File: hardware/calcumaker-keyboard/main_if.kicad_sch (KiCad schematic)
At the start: 2 parts, among them J1 TO MCU (stack), J3 TO MCU (FFC)

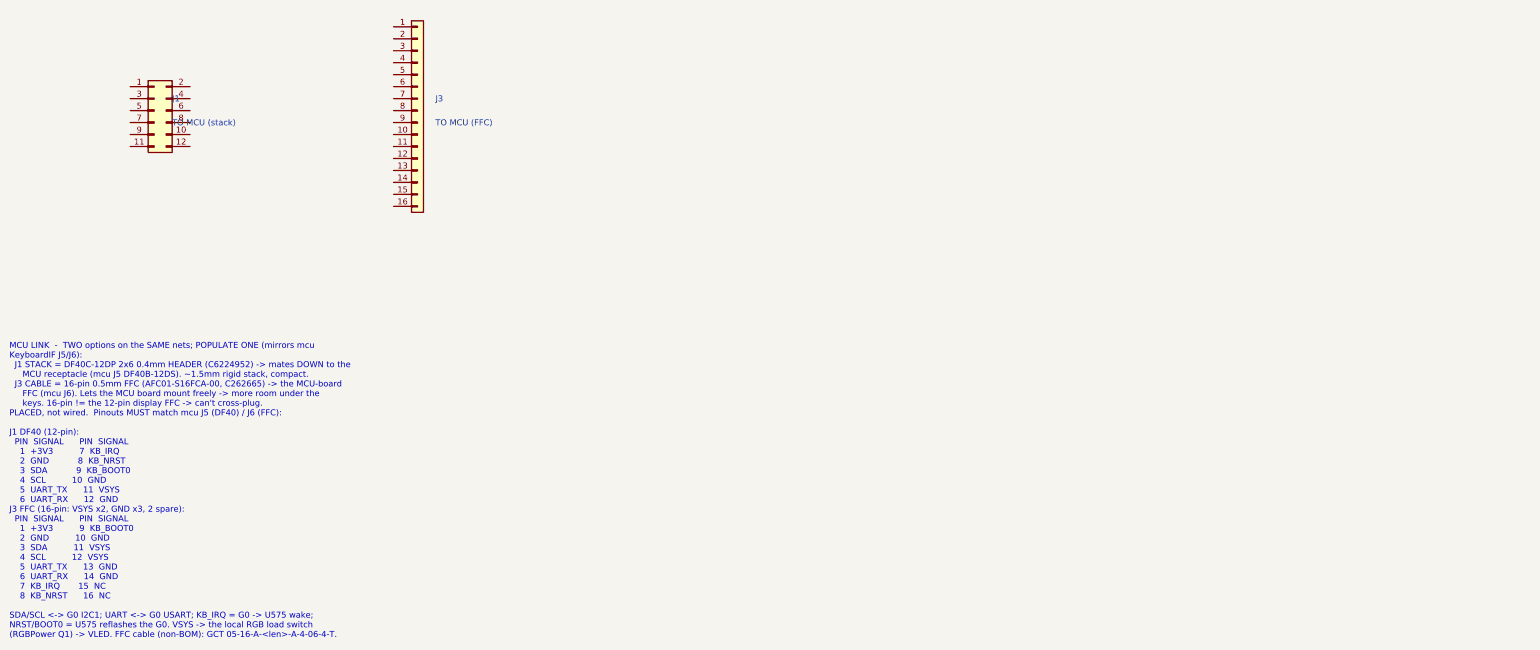
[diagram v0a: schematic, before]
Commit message: Wire mainboard and keypad schematics and verify expanded nets
Connect hierarchical interfaces, power/control circuits, debug links, matrix and RGB chains. Correct MCU package pins, diode polarity and power configuration; add bypass components and repeatable KiCad netlist/ERC checks. Document pin maps and remaining physical validation.
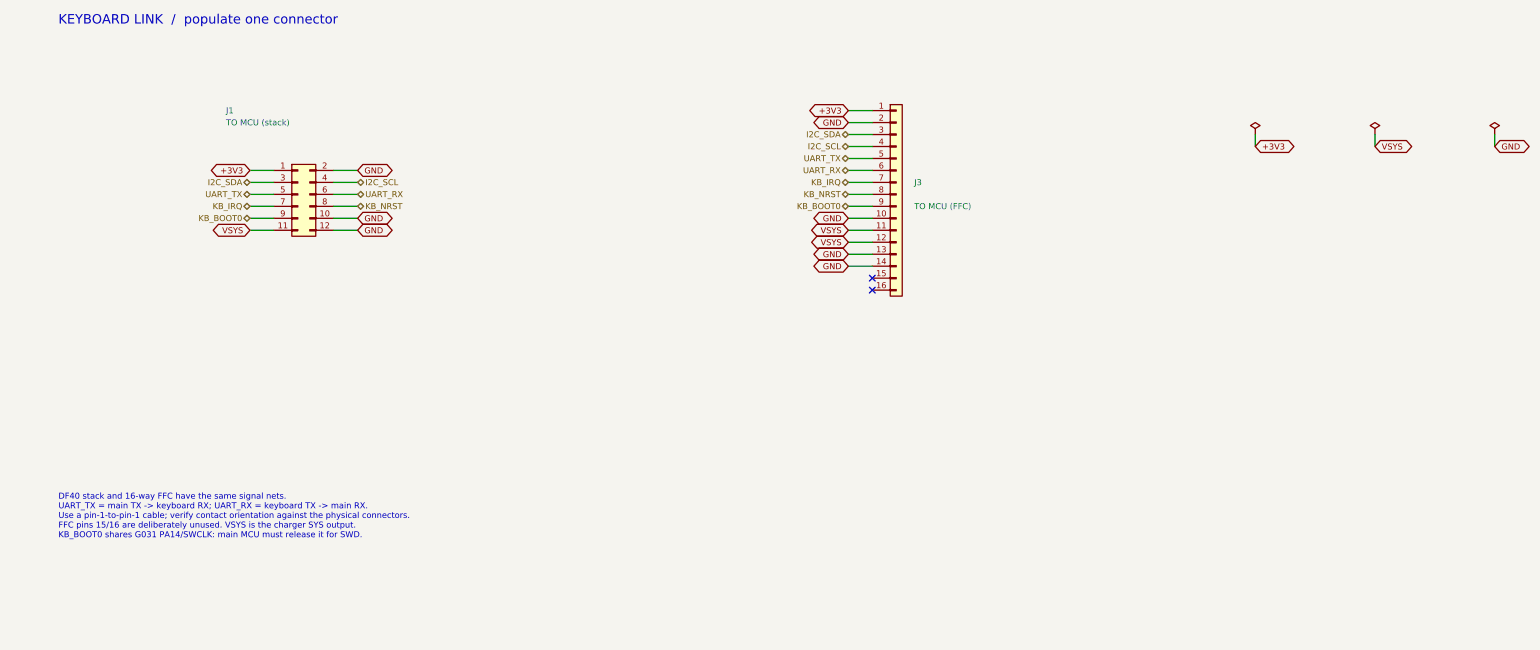
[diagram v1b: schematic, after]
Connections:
- net +3V3: now reaches J1.1 (Pin_1)
- net +3V3: now also J3.1 (Pin_1)
- net GND: now reaches J1.10 (Pin_10)
- net GND: now also J1.12 (Pin_12), J1.2 (Pin_2), J3.10 (Pin_10), J3.13 (Pin_13), J3.14 (Pin_14), J3.2 (Pin_2)
- net VSYS: now reaches J1.11 (Pin_11)
- net VSYS: now also J3.11 (Pin_11), J3.12 (Pin_12)
- net I2C_SDA: now reaches J1.3 (Pin_3)
- net I2C_SDA: now also J3.3 (Pin_3)
- net I2C_SCL: now reaches J1.4 (Pin_4)
- net I2C_SCL: now also J3.4 (Pin_4)
- net UART_TX: now reaches J1.5 (Pin_5)
- net UART_TX: now also J3.5 (Pin_5)
- net UART_RX: now reaches J1.6 (Pin_6)
- net UART_RX: now also J3.6 (Pin_6)
- net KB_IRQ: now reaches J1.7 (Pin_7)
- net KB_IRQ: now also J3.7 (Pin_7)
- net KB_NRST: now reaches J1.8 (Pin_8)
- net KB_NRST: now also J3.8 (Pin_8)
- net KB_BOOT0: now reaches J1.9 (Pin_9)
- net KB_BOOT0: now also J3.9 (Pin_9)
- no-connect marks 0 -> 2
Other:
- note added: "DF40 stack and 16-way FFC have the same signal nets. UART_TX = main TX -> keyboard RX; UART_RX = keyboard TX -> main RX. Use a pin-1-to-pin-1 cable; verify contact orientation against the physical connectors. FFC pins 15/16 are deliberately unused. VSYS is the charger SYS output. KB_BOOT0 shares G031 PA14/SWCLK: main MCU must release it for SWD."
- note added: "KEYBOARD LINK / populate one connector"
- note removed: "MCU LINK - TWO options on the SAME nets; POPULATE ONE (mirrors mcu KeyboardIF J5/J6): J1 STACK = DF40C-12DP 2x6 0.4mm HEADER (C6224952) -> mates DOWN to the MCU receptacle (mcu J5 DF40B-12DS). ~1.5mm rigid stack, compact. J3 CABLE = 16-pin 0.5mm FFC (AFC01-S16FCA-00, C262665) -> the MCU-board FFC (mcu J6). Lets the MCU board mount freely -> more room under the keys. 16-pin != the 12-pin display F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"
- title: Calcumaker 16 — Keyboard — MCU link -- DF40 stack (J1) OR 16-pin FFC (J3), populate one -> Calcumaker 16 / keyboard / main if
- moved on the sheet: J1, J3
